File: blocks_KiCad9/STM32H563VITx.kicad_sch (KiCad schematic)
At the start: 36 parts, among them Q14 NMOS_GSD, U15 UCC2946, U23 SN74AHC1G00

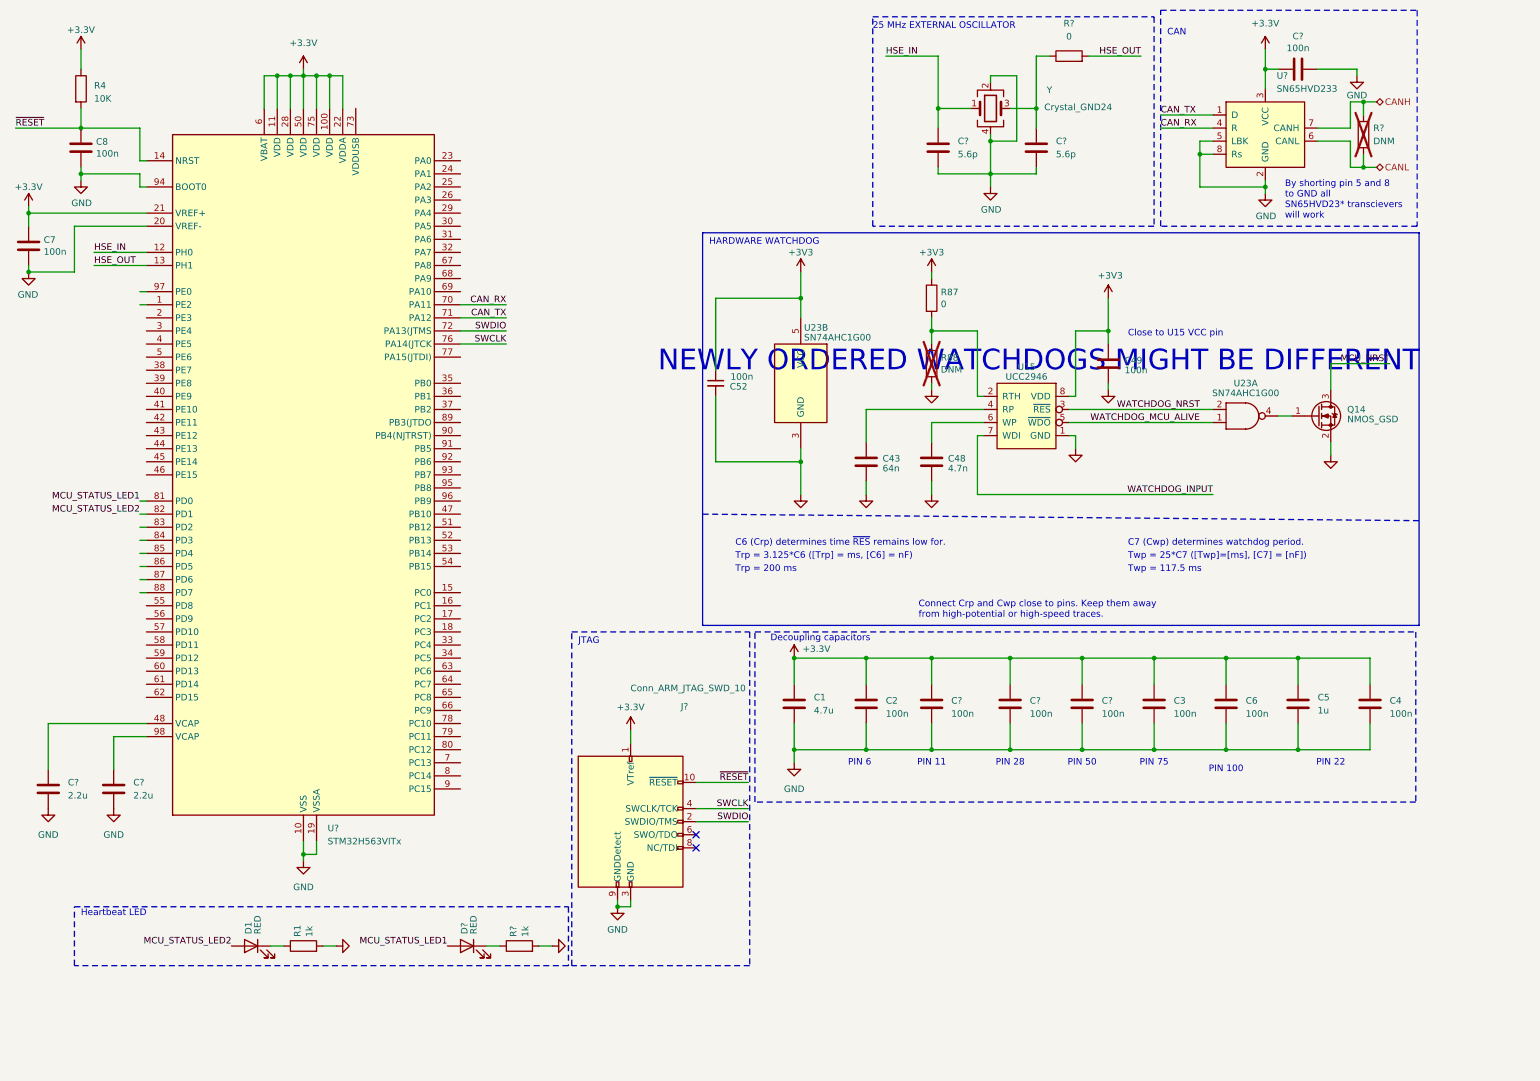
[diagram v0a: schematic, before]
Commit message: STM32H563VITx done (UNREVIEWED)
New hardware watchdog implementation and rest is done aswell.
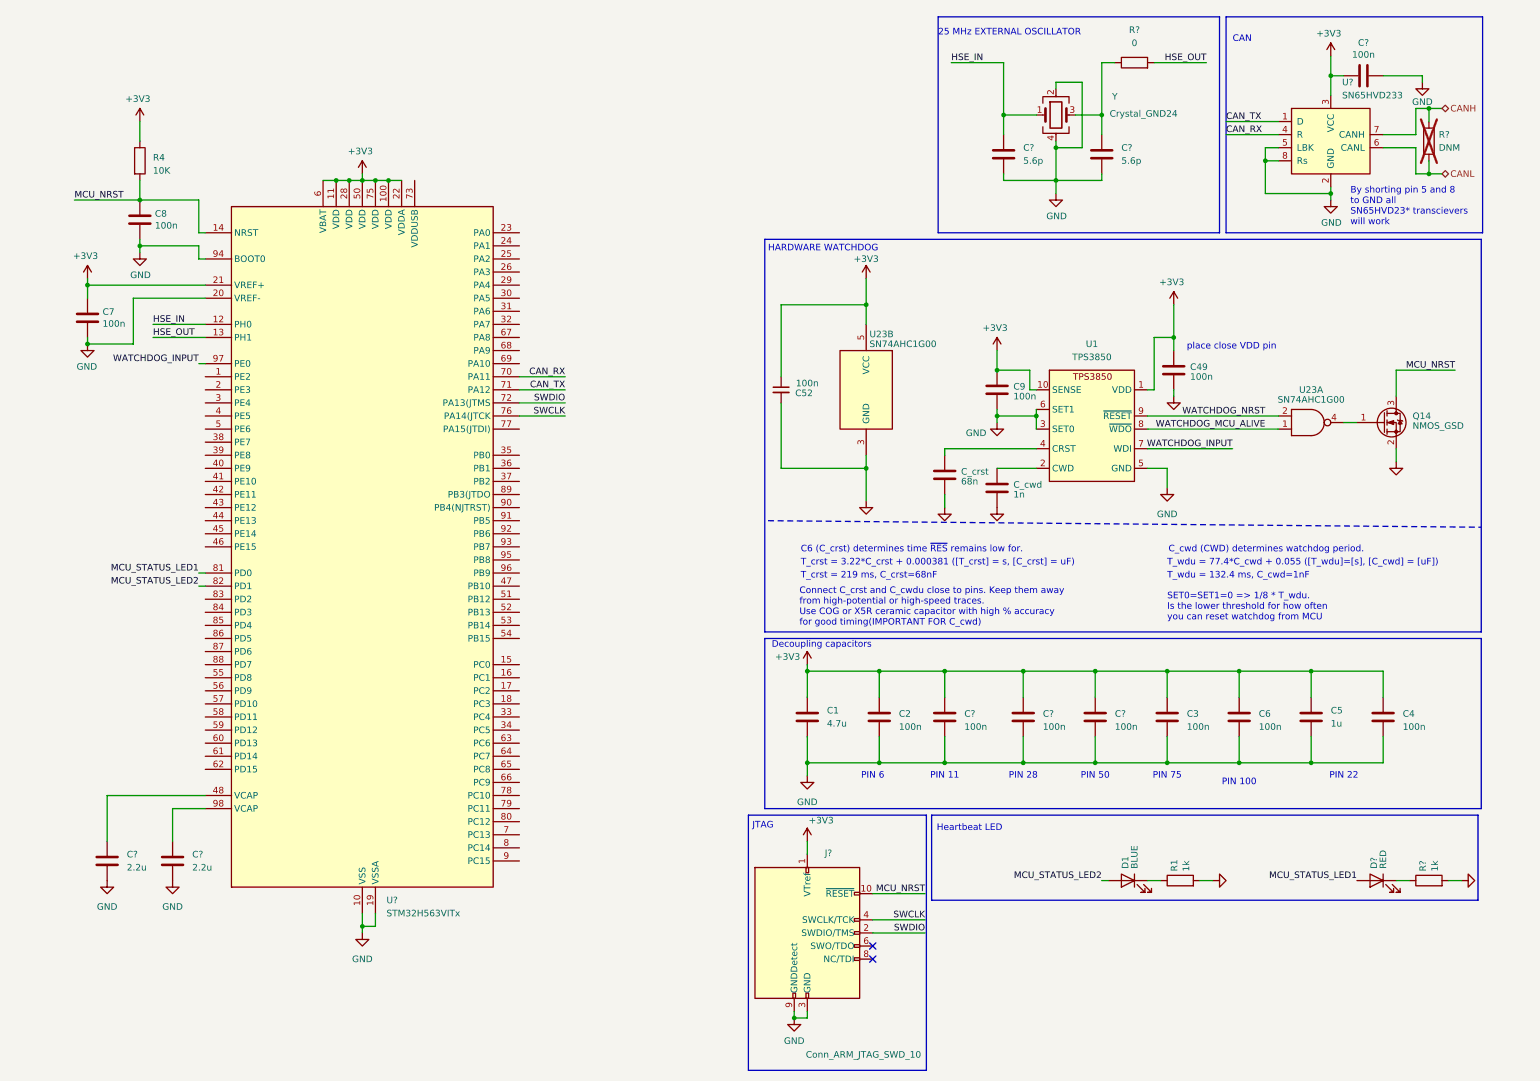
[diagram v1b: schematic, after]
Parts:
- removed R87: 0, Resistor_SMD:R_0603_1608Metric, symbol Device:R
- removed R88: DNM, Resistor_SMD:R_0603_1608Metric, symbol Device:R
- removed U15: UCC2946, Package_SO:SOIC-8_3.9x4.9mm_P1.27mm, symbol DeV18-AMS_bot_0.1-rescue:UCC2946-KTHFS
- added C9: 100n, Capacitor_SMD:C_0603_1608Metric, symbol Device:C
- added U1: TPS3850, Package_SON:VSON-10-1EP_3x3mm_P0.5mm_EP1.65x2.4mm, symbol KTHFS:TPS3850
- C_crst: renamed from C43; value 64n -> 68n
- C_cwd: renamed from C48; value 4.7n -> 1n
- D1: value RED -> BLUE
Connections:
- net +3.3V is gone; now on net +3V3: C1.1, C2.1, C3.1, C4.1, C5.1, C6.1, C7.1, C?.1, C?.1, C?.1, C?.2, J?.1 (VTref), R4.1, U?.100 (VDD), U?.11 (VDD), U?.21 (VREF+), U?.22 (VDDA), U?.28 (VDD), U?.3 (VCC), U?.50 (VDD), U?.6 (VBAT), U?.75 (VDD)
- net ~{RESET} is gone; now on net MCU_NRST: C8.1, J?.10 (~{RESET}), R4.2, U?.14 (NRST)
- net +3V3: now also C9.1, U1.1 (VDD), U1.10 (SENSE)
- net GND: now also C9.2, U1.3 (SET0), U1.5 (GND), U1.6 (SET1)
- net WATCHDOG_INPUT: now also U?.97 (PE0), U1.7 (WDI)
- net WATCHDOG_MCU_ALIVE: now also U1.8 (~{WDO})
- net WATCHDOG_NRST: now also U1.9 (~{RESET})
- net at C_crst.1: now also U1.4 (CRST)
- net at C_cwd.1: now also U1.2 (CWD)
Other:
- note added: "C6 (C_crst) determines time ~{RES} remains low for."
- note added: "C_cwd (CWD) determines watchdog period."
- note added: "Connect C_crst and C_cwdu close to pins. Keep them away from high-potential or high-speed traces. Use COG or X5R ceramic capacitor with high % accuracy for good timing(IMPORTANT FOR C_cwd)"
- note added: "SET0=SET1=0 => 1/8 * T_wdu. Is the lower threshold for how often you can reset watchdog from MCU"
- note added: "T_crst = 219 ms, C_crst=68nF"
- note added: "T_crst = 3.22*C_crst + 0.000381 ([T_crst] = s, [C_crst] = uF)"
- note added: "T_wdu = 132.4 ms, C_cwd=1nF"
- note added: "T_wdu = 77.4*C_cwd + 0.055 ([T_wdu]=[s], [C_cwd] = [uF])"
- note added: "place close VDD pin"
- note removed: "C6 (Crp) determines time ~{RES} remains low for."
- note removed: "C7 (Cwp) determines watchdog period."
- note removed: "Close to U15 VCC pin"
- note removed: "Connect Crp and Cwp close to pins. Keep them away from high-potential or high-speed traces."
- note removed: "NEWLY ORDERED WATCHDOGS MIGHT BE DIFFERENT"
- note removed: "Trp = 200 ms"
- note removed: "Trp = 3.125*C6 ([Trp] = ms, [C6] = nF)"
- note removed: "Twp = 117.5 ms"
- note removed: "Twp = 25*C7 ([Twp]=[ms], [C7] = [nF])"
- moved on the sheet: C1, C2, C3, C4, C49, C5, C52, C6, C7, C8, C?, C_crst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
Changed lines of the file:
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@@
 	(generator "eeschema")
 	(generator_version "9.0")
-	(paper "A4")
+	(paper "User" 310 230)
 	(title_block
 		(title "STM32H563VITx")

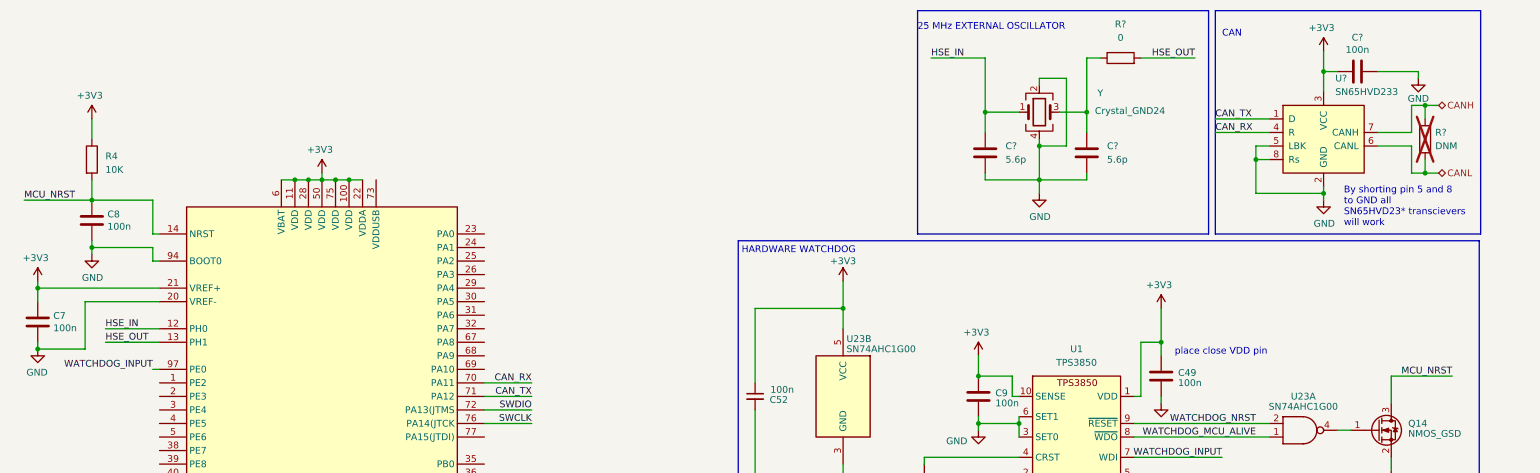
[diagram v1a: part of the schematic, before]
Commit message: small change to MCU
boot pin resistor  and jumper for debugging purposes
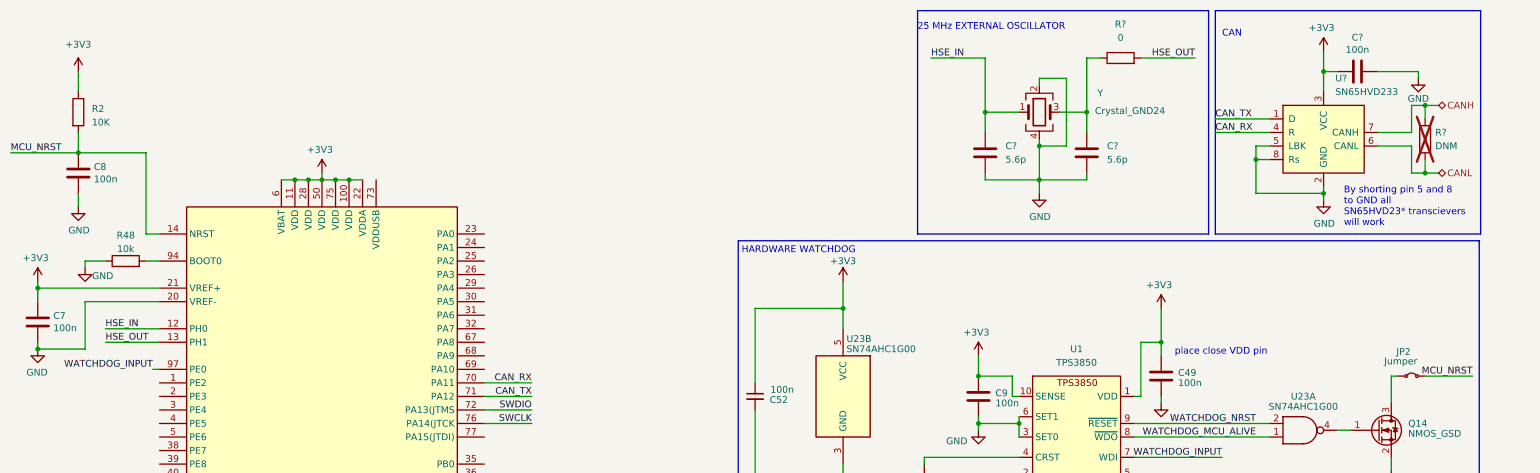
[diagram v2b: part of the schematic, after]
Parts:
- removed R4: 10K, Resistor_SMD:R_0603_1608Metric, symbol Device:R
- added JP2: Jumper, Connector_PinHeader_1.00mm:PinHeader_2x01_P1.00mm_Vertical, symbol Jumper:Jumper_2_Small_Bridged
- added R2: 10K, Resistor_SMD:R_0603_1608Metric, symbol Device:R
- added R48: 10k, Resistor_SMD:R_0603_1608Metric, symbol Device:R
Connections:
- net +3V3: now also R2.1
- net GND: now also R48.1; no longer U?.94 (BOOT0)
- net MCU_NRST: now also JP2.2 (B), R2.2; no longer Q14.3 (D)
- new net: R48.2, U?.94 (BOOT0)
- new net: JP2.1 (A), Q14.3 (D)

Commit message: forgot footprint mcu
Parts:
- C? (x2): footprint (none) -> Capacitor_SMD:C_0805_2012Metric
